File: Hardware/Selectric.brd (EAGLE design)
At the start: 101.5 x 53.3 mm, 117 parts, among them IC1 MAX3232ESE, Q1 BSP613P, Q10 BSS123, Q11 BSP613P, Q12 BSS123, Q13 BSP613P, Q14 BSS123, Q15 BSP613P, Q16 BSS123, Q17 BSP613P, Q18 BSS123, Q19 BSP613P, Q2 BSS123, Q20 BSS123, Q21 BSP613P, Q22 BSS123, Q23 BSP613P, Q24 BSS123, Q25 BSP613P, Q26 BSS123, Q27 BSP613P, Q28 BSS123, Q29 BSP613P, Q3 BSP613P, Q30 BSS123, Q31 BSP613P, Q32 BSS123, Q4 BSS123, Q5 BSP613P, Q6 BSS123, Q7 BSP613P, Q8 BSS123, Q9 BSP613P

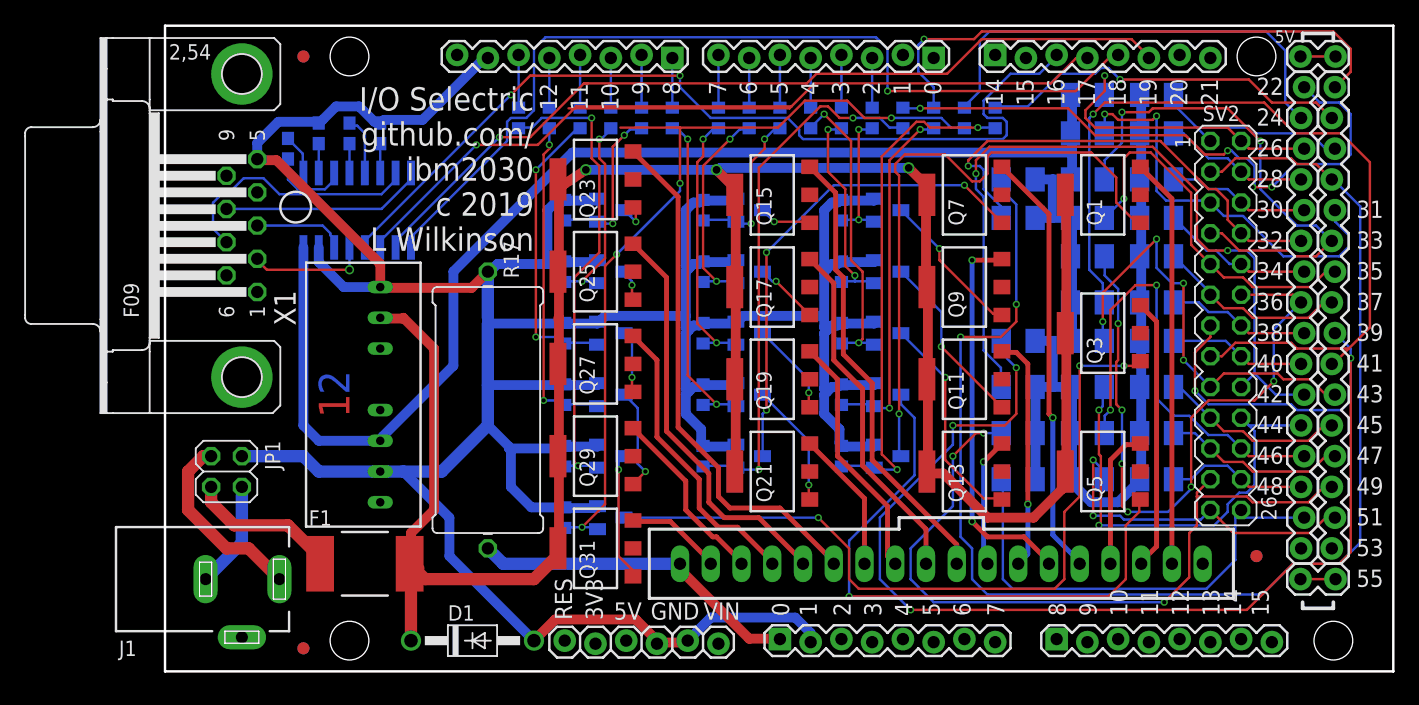
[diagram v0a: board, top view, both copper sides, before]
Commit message: Updated schematic and tidied board
Added Arduino 5V power feed. Tidied some traces and labels.
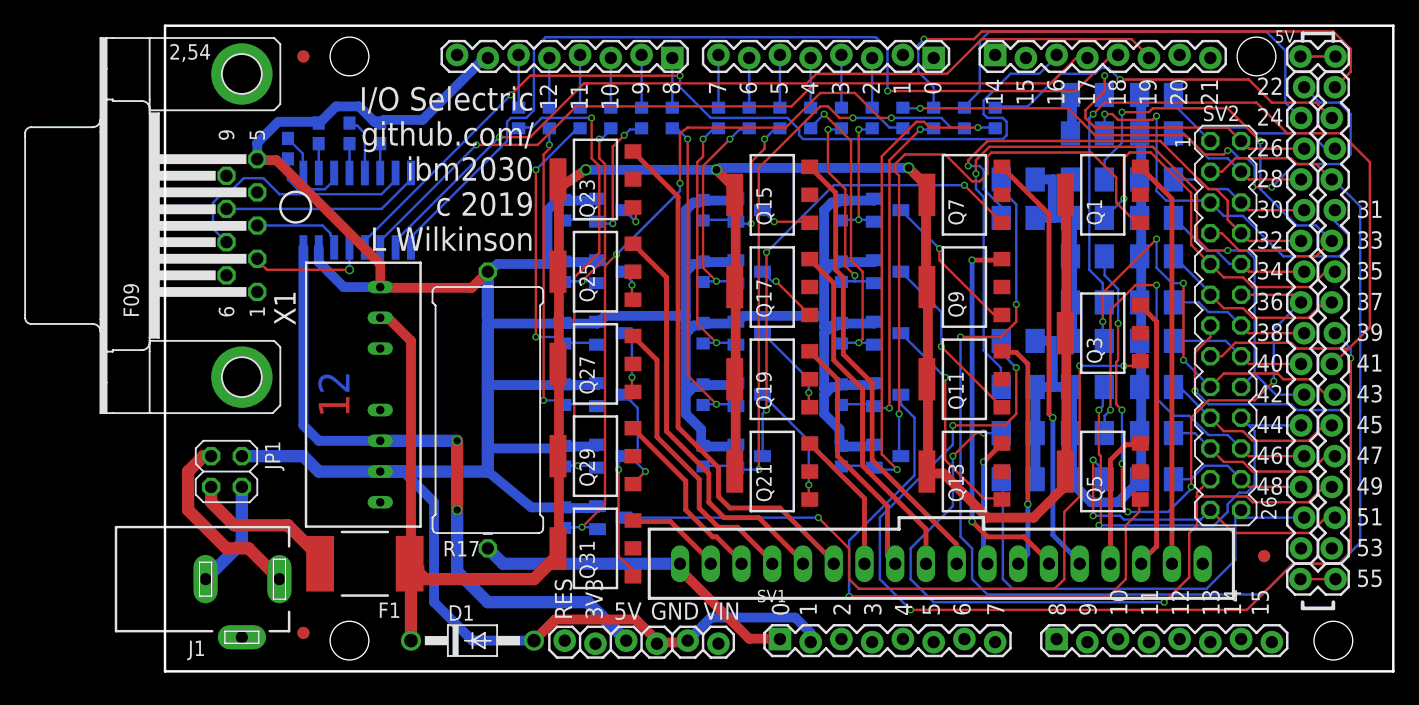
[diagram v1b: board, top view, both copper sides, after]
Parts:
- moved U$1 1.27 mm to (11.4, 3.17)
- moved U$2 0.64 mm to (90.8, 9.53)
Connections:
- net 5V: now also DC1.6, IC1.16
- net VCC: no longer DC1.6, IC1.16
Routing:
- net VCC: track 186.1 -> 89.0 mm
- net 5V: track 0.00 -> 55.1 mm, vias 0 -> 2
- net TX1: track 83.7 -> 65.2 mm
- net GND: track 294.0 -> 299.3 mm
- net N$8: track 69.6 -> 64.9 mm
- net HSDCOM: track 197.9 -> 195.7 mm

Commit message: Adjust some screen labels for tidiness
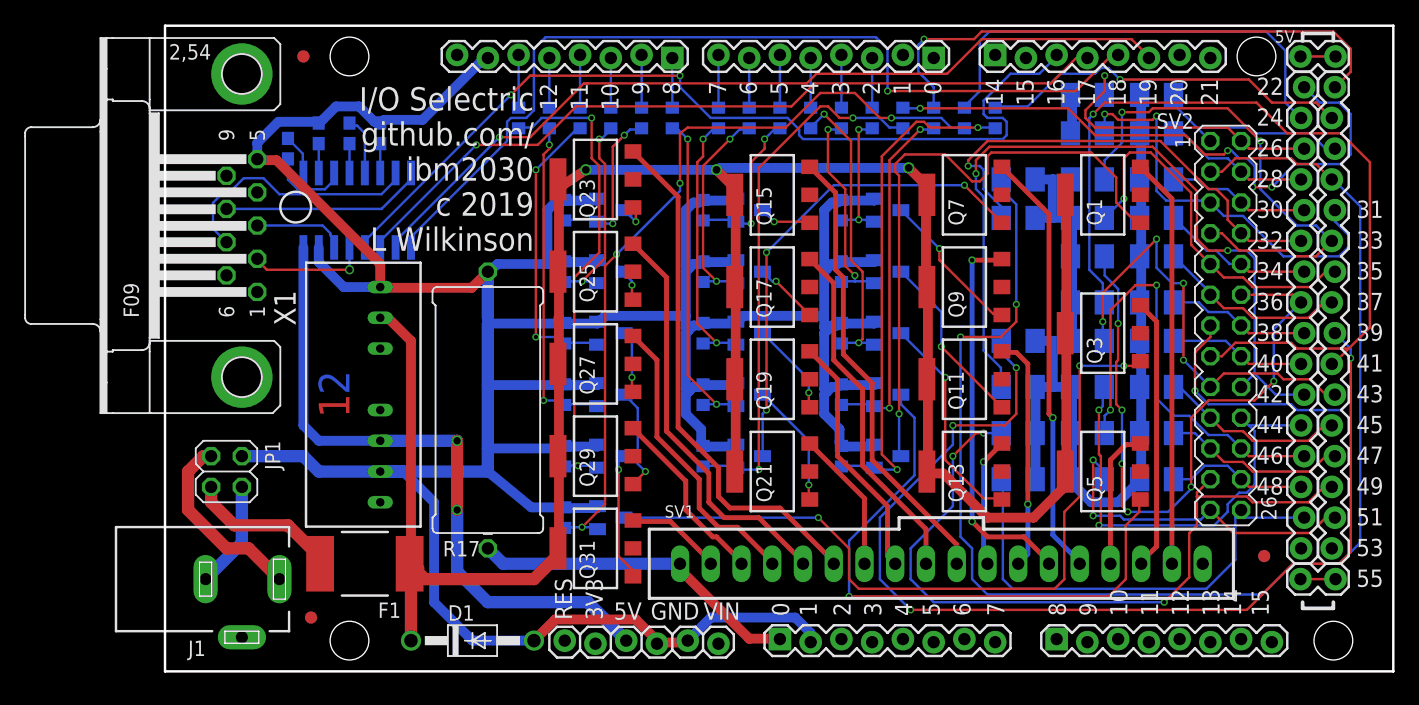
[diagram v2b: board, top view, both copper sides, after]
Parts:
- moved U$1 1.42 mm to (12.1, 4.45)
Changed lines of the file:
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@@
 <layers>
 <layer number="1" name="Top" color="4" fill="1" visible="yes" active="yes"/>
-<layer number="2" name="Route2" color="10" fill="3" visible="no" active="yes"/>
-<layer number="3" name="Route3" color="11" fill="3" visible="no" active="yes"/>
+<layer number="2" name="Route2" color="10" fill="3" visible="yes" active="yes"/>
+<layer number="3" name="Route3" color="11" fill="3" visible="yes" active="yes"/>
 <layer number="4" name="Route4" color="1" fill="4" visible="no" active="no"/>
 <layer number="5" name="Route5" color="4" fill="4" visible="no" active="no"/>
@@
 <layer number="14" name="Route14" color="1" fill="6" visible="no" active="no"/>
 <layer number="15" name="Route15" color="13" fill="6" visible="no" active="no"/>
-<layer number="16" name="Bottom" color="1" fill="1" visible="no" active="yes"/>
+<layer number="16" name="Bottom" color="1" fill="1" visible="yes" active="yes"/>
 <layer number="17" name="Pads" color="2" fill="1" visible="yes" active="yes"/>
 <layer number="18" name="Vias" color="2" fill="1" visible="yes" active="yes"/>
-<layer number="19" name="Unrouted" color="6" fill="1" visible="no" active="yes"/>
-<layer number="20" name="Dimension" color="15" fill="1" visible="yes" active="yes"/>
-<layer number="21" name="tPlace" color="16" fill="1" visible="no" active="yes"/>
-<layer number="22" name="bPlace" color="14" fill="1" visible="no" active="yes"/>
+<layer number="19" name="Unrouted" color="6" fill="1" visible="yes" active="yes"/>
+<layer number="20" name="Dimension" color="15" fill="1" visible="no" active="yes"/>
+<layer number="21" name="tPlace" color="16" fill="1" visible="yes" active="yes"/>
+<layer number="22" name="bPlace" color="14" fill="1" visible="yes" active="yes"/>
 <layer number="23" name="tOrigins" color="15" fill="1" visible="yes" active="yes"/>
-<layer number="24" name="bOrigins" color="15" fill="1" visible="no" active="yes"/>
+<layer number="24" name="bOrigins" color="15" fill="1" visible="yes" active="yes"/>
 <layer number="25" name="tNames" color="7" fill="1" visible="yes" active="yes"/>
-<layer number="26" name="bNames" color="7" fill="1" visible="no" active="yes"/>
-<layer number="27" name="tValues" color="7" fill="1" visible="no" active="yes"/>
-<layer number="28" name="bValues" color="7" fill="1" visible="no" active="yes"/>
+<layer number="26" name="bNames" color="7" fill="1" visible="yes" active="yes"/>
+<layer number="27" name="tValues" color="7" fill="1" visible="yes" active="yes"/>
+<layer number="28" name="bValues" color="7" fill="1" visible="yes" active="yes"/>
 <layer number="29" name="tStop" color="7" fill="3" visible="yes" active="yes"/>
-<layer number="30" name="bStop" color="7" fill="6" visible="no" active="yes"/>
+<layer number="30" name="bStop" color="7" fill="6" visible="yes" active="yes"/>
 <layer number="31" name="tCream" color="7" fill="4" visible="yes" active="yes"/>
-<layer number="32" name="bCream" color="7" fill="5" visible="no" active="yes"/>
+<layer number="32" name="bCream" color="7" fill="5" visible="yes" active="yes"/>
 <layer number="33" name="tFinish" color="6" fill="3" visible="yes" active="yes"/>
-<layer number="34" name="bFinish" color="6" fill="6" visible="no" active="yes"/>
+<layer number="34" name="bFinish" color="6" fill="6" visible="yes" active="yes"/>
 <layer number="35" name="tGlue" color="7" fill="4" visible="yes" active="yes"/>
-<layer number="36" name="bGlue" color="7" fill="5" visible="no" active="yes"/>
+<layer number="36" name="bGlue" color="7" fill="5" visible="yes" active="yes"/>
 <layer number="37" name="tTest" color="7" fill="1" visible="yes" active="yes"/>
-<layer number="38" name="bTest" color="7" fill="1" visible="no" active="yes"/>
+<layer number="38" name="bTest" color="7" fill="1" visible="yes" active="yes"/>
 <layer number="39" name="tKeepout" color="4" fill="11" visible="yes" active="yes"/>
-<layer number="40" name="bKeepout" color="1" fill="11" visible="no" active="yes"/>
+<layer number="40" name="bKeepout" color="1" fill="11" visible="yes" active="yes"/>
 <layer number="41" name="tRestrict" color="4" fill="10" visible="yes" active="yes"/>
-<layer number="42" name="bRestrict" color="1" fill="10" visible="no" active="yes"/>
+<layer number="42" name="bRestrict" color="1" fill="10" visible="yes" active="yes"/>
 <layer number="43" name="vRestrict" color="2" fill="10" visible="no" active="yes"/>
 <layer number="44" name="Drills" color="7" fill="1" visible="no" active="yes"/>
@@
 <layer number="116" name="Patch_BOT" color="9" fill="4" visible="no" active="yes"/>
 <layer number="121" name="_tsilk" color="7" fill="1" visible="yes" active="yes"/>
-<layer number="122" name="_bsilk" color="7" fill="1" visible="no" active="yes"/>
+<layer number="122" name="_bsilk" color="7" fill="1" visible="yes" active="yes"/>
 <layer number="151" name="HeatSink" color="7" fill="1" visible="no" active="yes"/>
 <layer number="200" name="200bmp" color="1" fill="10" visible="no" active="yes"/>
@@
 </element>
 <element name="R10" library="rcl" package="R0603" value="1M0" x="55.88" y="38.1" smashed="yes" rot="MR90">
-<attribute name="NAME" x="53.34" y="36.83" size="1.27" layer="26" rot="MR90"/>
+<attribute name="NAME" x="53.34" y="36.195" size="1.27" layer="26" rot="MR90"/>
 <attribute name="VALUE" x="53.975" y="37.465" size="1.27" layer="28" rot="MR90"/>
 </element>
@@
 <attribute name="MF" value="" x="64.135" y="8.89" size="1.778" layer="27" rot="R180" display="off"/>
 <attribute name="OC_FARNELL" value="unknown" x="64.135" y="8.89" size="1.778" layer="27" rot="R180" display="off"/>
-<attribute name="NAME" x="48.895" y="5.715" size="1.016" layer="25" ratio="10"/>
+<attribute name="NAME" x="41.275" y="12.7" size="1.016" layer="25" ratio="10"/>
 <attribute name="VALUE" x="87.9475" y="5.3975" size="0.8128" layer="27" ratio="10" rot="R180"/>
 </element>
@@
 <attribute name="MF" value="" x="87.63" y="28.575" size="1.778" layer="27" rot="R270" display="off"/>
 <attribute name="OC_FARNELL" value="unknown" x="87.63" y="28.575" size="1.778" layer="27" rot="R270" display="off"/>
-<attribute name="NAME" x="85.725" y="45.466" size="1.27" layer="25" ratio="10"/>
+<attribute name="NAME" x="81.915" y="44.831" size="1.27" layer="25" ratio="10"/>
 <attribute name="VALUE" x="83.439" y="20.955" size="1.27" layer="27" ratio="10" rot="R270"/>
 </element>
@@
 </element>
 <element name="R36" library="rcl" package="M1206" value="220R" x="70.485" y="40.64" smashed="yes" rot="MR0">
-<attribute name="NAME" x="67.945" y="39.37" size="1.27" layer="26" rot="MR0"/>
+<attribute name="NAME" x="73.025" y="41.91" size="1.27" layer="26" rot="MR0"/>
 <attribute name="VALUE" x="71.755" y="38.1" size="1.27" layer="28" rot="MR0"/>
 </element>
@@
 </element>
 <element name="R38" library="rcl" package="M1206" value="220R" x="76.2" y="44.45" smashed="yes" rot="MR180">
-<attribute name="NAME" x="74.93" y="43.18" size="1.27" layer="26" rot="MR180"/>
+<attribute name="NAME" x="69.85" y="46.355" size="1.27" layer="26" rot="MR180"/>
 <attribute name="VALUE" x="74.93" y="46.99" size="1.27" layer="28" rot="MR180"/>
 </element>
@@
 </element>
 <element name="R40" library="rcl" package="M1206" value="220R" x="76.2" y="40.64" smashed="yes" rot="MR180">
-<attribute name="NAME" x="69.85" y="43.18" size="1.27" layer="26" rot="MR180"/>
+<attribute name="NAME" x="77.47" y="41.91" size="1.27" layer="26" rot="MR0"/>
 <attribute name="VALUE" x="74.93" y="43.18" size="1.27" layer="28" rot="MR180"/>
 </element>
@@
 <element name="U$2" library="fiducial" package="CIRCLE-1MM-3R" value="" x="90.805" y="9.525"/>
 <element name="U$3" library="fiducial" package="CIRCLE-1MM-3R" value="" x="11.43" y="50.8"/>
-<element name="U$1" library="fiducial" package="CIRCLE-1MM-3R" value="" x="11.43" y="3.175"/>
+<element name="U$1" library="fiducial" package="CIRCLE-1MM-3R" value="" x="12.065" y="4.445"/>
 </elements>
 <signals>

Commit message: Modify to use Allegro A2982SLW-T drivers
Replace discrete mosfets with A2982 driver ICs.
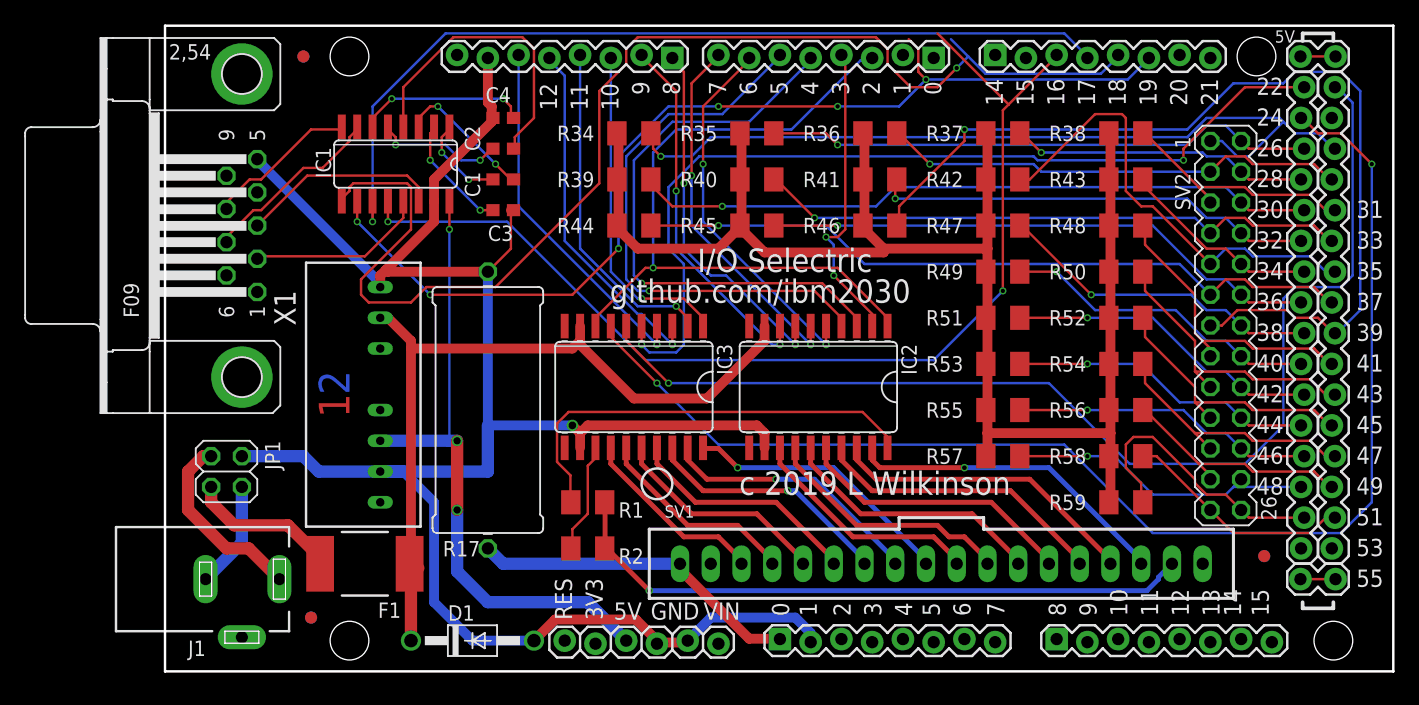
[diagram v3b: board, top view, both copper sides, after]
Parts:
- removed Q1, Q11, Q13, Q15, Q17, Q19, Q21, Q23, Q25, Q27, Q29, Q3, Q31, Q5, Q7, Q9: BSP613P, infineon:PG-SOT-223
- removed Q10, Q12, Q14, Q16, Q18, Q2, Q20, Q22, Q24, Q26, Q28, Q30, Q32, Q4, Q6, Q8: BSS123, transistor-small-signal:SOT23
- removed R10, R12, R14, R16, R19, R21, R23, R25, R27, R29, R31, R33, R4, R6, R8: 1M0, rcl:R0603
- removed R11, R13, R15, R18, R20, R22, R24, R26, R28, R3, R30, R32, R5, R7, R9: 1K0, rcl:R0603
- added IC2, IC3: UDN2982SLW, uln-udn:SO20W
- R1: value 1K0 -> 10R; device rcl:R0603 -> rcl:M1206
- R2: value 1M0 -> 10R; device rcl:R0603 -> rcl:M1206
- moved R1 46.3 mm to (34.9, 14.0), flipped to the top, turned to 0 degrees
- moved R34 43.3 mm to (38.7, 44.5), flipped to the top, turned to 0 degrees
- moved R44 43.3 mm to (38.7, 36.8), flipped to the top, turned to 0 degrees
- moved R39 43.2 mm to (38.7, 40.6), flipped to the top, turned to 180 degrees
- moved R35 27.5 mm to (48.9, 44.5), flipped to the top, turned to 180 degrees
- moved R45 27.4 mm to (48.9, 36.8), flipped to the top, turned to 180 degrees
- moved R40 27.3 mm to (48.9, 40.6), flipped to the top, turned to 0 degrees
- moved R2 22.3 mm to (34.9, 10.2), flipped to the top, turned to 0 degrees
- moved C1 18.0 mm to (27.9, 40.6), flipped to the top, turned to 0 degrees
- moved C3 16.5 mm to (27.9, 38.1), flipped to the top, turned to 0 degrees
- moved R46 14.9 mm to (59.1, 36.8), flipped to the top
- moved R47 14.2 mm to (69.2, 36.8), flipped to the top, turned to 180 degrees
- moved R49 13.9 mm to (69.2, 33.0), flipped to the top, turned to 180 degrees
- moved R57 12.8 mm to (69.2, 17.8), flipped to the top, turned to 180 degrees
- moved C2 12.8 mm to (27.9, 43.2), flipped to the top, turned to 180 degrees
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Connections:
- removed net N$10: Q3.1, Q4.3
- removed net N$11: Q6.1, R5.2, R6.1
- removed net N$12: Q5.1, Q6.3
- removed net N$13: Q8.1, R7.2, R8.1
- removed net N$14: Q7.1, Q8.3
- removed net N$15: Q10.1, R10.1, R9.2
- removed net N$16: Q10.3, Q9.1
- removed net N$17: Q12.1, R11.2, R12.1
- removed net N$18: Q11.1, Q12.3
- removed net N$19: Q14.1, R13.2, R14.1
- removed net N$20: Q13.1, Q14.3
- removed net N$21: Q16.1, R15.2, R16.1
- removed net N$22: Q15.1, Q16.3
- removed net N$26: Q18.1, R18.2, R19.1
- removed net N$27: Q17.1, Q18.3
- removed net N$28: Q20.1, R20.2, R21.1
- removed net N$29: Q19.1, Q20.3
- removed net N$30: Q22.1, R22.2, R23.1
- removed net N$31: Q21.1, Q22.3
- removed net N$32: Q24.1, R24.2, R25.1
- removed net N$33: Q23.1, Q24.3
- removed net N$34: Q26.1, R26.2, R27.1
- removed net N$35: Q25.1, Q26.3
- removed net N$36: Q28.1, R28.2, R29.1
- removed net N$37: Q27.1, Q28.3
- removed net N$38: Q30.1, R30.2, R31.1
- removed net N$39: Q29.1, Q30.3
- removed net N$40: Q32.1, R32.2, R33.1
- removed net N$41: Q31.1, Q32.3
- removed net N$9: Q1.1, Q2.3
- net D10: now also IC3.1; no longer R26.1
- net D11: now also IC3.2; no longer R28.1
- net D12: now also IC3.3; no longer R30.1
- net D13: now also IC3.4; no longer R32.1
- net D2: now also IC2.1, IC3.8; no longer R9.1
- net D22: now also IC3.5; no longer R7.1
- net D23: now also IC3.6; no longer R5.1
- net D24: now also IC3.7; no longer R3.1
- net D25: no longer R1.1
- net D3: now also IC2.2; no longer R11.1
- net D4: now also IC2.3; no longer R13.1
- net D5: now also IC2.4; no longer R15.1
- net D6: now also IC2.5; no longer R18.1
- net D7: now also IC2.6; no longer R20.1
- net D8: now also IC2.7; no longer R22.1
- net D9: now also IC2.8; no longer R24.1
- net GND: now also IC2.12, IC3.12; no longer Q10.2, Q12.2, Q14.2, Q16.2, Q18.2, Q2.2, Q20.2, Q22.2, Q24.2, Q26.2, Q28.2, Q30.2, Q32.2, Q4.2, Q6.2, Q8.2, R10.2, R12.2, R14.2, R16.2, R19.2, R2.2, R21.2, R23.2, R25.2, R27.2, R29.2, R31.2, R33.2, R4.2, R6.2, R8.2
- net HSD1: now also R1.2, R2.2; no longer Q1.3
- net HSD10: now also IC3.19; no longer Q19.3
- net HSD11: now also IC3.18; no longer Q21.3
- net HSD12: now also IC3.17; no longer Q23.3
- net HSD13: now also IC3.16; no longer Q25.3
- net HSD14: now also IC3.15; no longer Q27.3
- net HSD15: now also IC3.14; no longer Q29.3
- net HSD16: no longer Q31.3
- net HSD2: now also IC2.19; no longer Q3.3
- net HSD3: now also IC2.18; no longer Q5.3
- net HSD4: now also IC2.17; no longer Q7.3
- net HSD5: now also IC2.16; no longer Q9.3
- net HSD6: now also IC2.15; no longer Q11.3
- net HSD7: now also IC2.14; no longer Q13.3
- net HSD8: now also IC2.13; no longer Q15.3
- net HSD9: now also IC3.20; no longer Q17.3
- net HSDCOM: now also IC2.9, IC3.9; no longer Q1.4, Q11.4, Q13.4, Q15.4, Q17.4, Q19.4, Q21.4, Q23.4, Q25.4, Q27.4, Q29.4, Q3.4, Q31.4, Q5.4, Q7.4, Q9.4
- net N$5: now also IC3.13; no longer Q2.1, R1.2
- net N$8: now also IC2.20, R1.1; no longer Q4.1, R3.2, R4.1
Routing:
- net GND: track 299.3 -> 165.9 mm, vias 0 -> 1
- net HSDCOM: track 195.7 -> 66.7 mm, vias 3 -> 0
- net D29: track 114.5 -> 38.6 mm, vias 2 -> 1
- net D24: track 38.4 -> 106.9 mm, vias 0 -> 2
- net N$10: track 63.9 -> 0.00 mm, vias 3 -> 0
- net D2: track 4.10 -> 59.9 mm, vias 0 -> 1
- net N$9: track 51.3 -> 0.00 mm, vias 1 -> 0
- net D27: track 17.2 -> 68.2 mm, vias 0 -> 1
- net N$12: track 49.9 -> 0.00 mm, vias 1 -> 0
- net D23: track 46.2 -> 94.3 mm
- net D41: track 71.7 -> 24.7 mm, vias 1 -> 0
- net D30: track 11.8 -> 56.7 mm, vias 0 -> 1
- net N$13: track 44.6 -> 0.00 mm, vias 2 -> 0
- net D4: track 4.10 -> 48.3 mm, vias 0 -> 1
- net D37: track 15.8 -> 59.9 mm, vias 0 -> 1
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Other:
- board text added: "I/O Selectric"
- board text added: "c 2019 L Wilkinson"
- board text added: "github.com/ibm2030"
- board text removed: "I/O Selectric github.com/ ibm2030 c 2019 L Wilkinson"
